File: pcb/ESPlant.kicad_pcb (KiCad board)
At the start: 2 copper layers, 43 x 23 mm, 23 parts, among them J1 Power, J2 TAG, J3 PUMP, J4 Soil Moisture, Q1 Q_NPN_BCE, Q2 Pump Driver, U1 ESP32-WROOM-32, U2 Si7021-A20, U3 LD1117S33TR_SOT223

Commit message: Increase with of pump traces to support 1A
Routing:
- net PUMP+: track 13.8 -> 14.8 mm
- net PUMP-: track 7.31 -> 8.27 mm
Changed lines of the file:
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@@
     (thickness 1.6)
     (drawings 4)
-    (tracks 157)
+    (tracks 161)
     (zones 0)
     (modules 23)
@@
   )
   (setup
-    (last_trace_width 0.25)
+    (last_trace_width 0.8)
+    (user_trace_width 0.8)
     (trace_clearance 0.2)
     (zone_clearance 0.508)
@@
     (add_net "Net-(Q1-Pad1)")
     (add_net "Net-(Q1-Pad2)")
-    (add_net "Net-(U1-Pad10)")
-    (add_net "Net-(U1-Pad13)")
-    (add_net "Net-(U1-Pad14)")
-    (add_net "Net-(U1-Pad16)")
-    (add_net "Net-(U1-Pad17)")
-    (add_net "Net-(U1-Pad18)")
-    (add_net "Net-(U1-Pad19)")
-    (add_net "Net-(U1-Pad20)")
-    (add_net "Net-(U1-Pad21)")
-    (add_net "Net-(U1-Pad22)")
-    (add_net "Net-(U1-Pad23)")
-    (add_net "Net-(U1-Pad24)")
-    (add_net "Net-(U1-Pad26)")
-    (add_net "Net-(U1-Pad27)")
-    (add_net "Net-(U1-Pad28)")
-    (add_net "Net-(U1-Pad29)")
-    (add_net "Net-(U1-Pad30)")
-    (add_net "Net-(U1-Pad31)")
-    (add_net "Net-(U1-Pad32)")
-    (add_net "Net-(U1-Pad37)")
-    (add_net "Net-(U1-Pad4)")
-    (add_net "Net-(U1-Pad5)")
-    (add_net "Net-(U2-Pad3)")
-    (add_net "Net-(U2-Pad4)")
-    (add_net "Net-(U2-Pad7)")
     (add_net PUMP+)
     (add_net PUMP-)
@@
   (segment (start 138 93.495) (end 138.75 92.745) (width 0.25) (layer F.Cu) (net 10))
   (segment (start 167.04 106.5) (end 168 106.5) (width 0.25) (layer B.Cu) (net 11))
-  (segment (start 165 104.46) (end 167.04 106.5) (width 0.25) (layer B.Cu) (net 11))
-  (segment (start 169.88 106.5) (end 171 107.62) (width 0.25) (layer B.Cu) (net 11))
-  (segment (start 168 106.5) (end 169.88 106.5) (width 0.25) (layer B.Cu) (net 11))
-  (segment (start 168.92 103) (end 168 103) (width 0.25) (layer B.Cu) (net 12))
-  (segment (start 171 105.08) (end 168.92 103) (width 0.25) (layer B.Cu) (net 12))
-  (segment (start 171 100) (end 168 103) (width 0.25) (layer B.Cu) (net 12))
-  (segment (start 167.475 98) (end 167 98) (width 0.25) (layer B.Cu) (net 12))
-  (segment (start 168 98.525) (end 167.475 98) (width 0.25) (layer B.Cu) (net 12))
-  (segment (start 168 103) (end 168 98.525) (width 0.25) (layer B.Cu) (net 12))
+  (segment (start 169.12 107.62) (end 168 106.5) (width 0.8) (layer B.Cu) (net 11))
+  (segment (start 171 107.62) (end 169.12 107.62) (width 0.8) (layer B.Cu) (net 11))
+  (segment (start 165.96 104.46) (end 168 106.5) (width 0.8) (layer B.Cu) (net 11))
+  (segment (start 165 104.46) (end 165.96 104.46) (width 0.8) (layer B.Cu) (net 11))
+  (segment (start 169.35 100) (end 168 101.35) (width 0.8) (layer B.Cu) (net 12))
+  (segment (start 168 101.35) (end 168 103) (width 0.8) (layer B.Cu) (net 12))
+  (segment (start 171 100) (end 169.35 100) (width 0.8) (layer B.Cu) (net 12))
+  (segment (start 168 102.1) (end 168 103) (width 0.25) (layer B.Cu) (net 12))
+  (segment (start 168 98.525) (end 168 102.1) (width 0.25) (layer B.Cu) (net 12))
+  (segment (start 167.475 98) (end 168 98.525) (width 0.25) (layer B.Cu) (net 12))
+  (segment (start 167 98) (end 167.475 98) (width 0.25) (layer B.Cu) (net 12))
+  (segment (start 170.08 105.08) (end 168 103) (width 0.8) (layer B.Cu) (net 12))
+  (segment (start 171 105.08) (end 170.08 105.08) (width 0.8) (layer B.Cu) (net 12))
   (via (at 159 98) (size 0.8) (drill 0.4) (layers F.Cu B.Cu) (net 13))
   (segment (start 157.875 99.125) (end 159 98) (width 0.25) (layer B.Cu) (net 13))
@@
   (segment (start 157 95.285) (end 158.715 95.285) (width 0.25) (layer F.Cu) (net 19))
   (segment (start 159 95) (end 152 95) (width 0.25) (layer B.Cu) (net 19))
+  (zone (net 1) (net_name GNDREF) (layer B.Cu) (hatch edge 0.508)
+    (connect_pads (clearance 0.508))
+    (min_thickness 0.254)
+    (fill yes (arc_segments 32) (thermal_gap 0.508) (thermal_bridge_width 0.508))
+    (polygon
+      (pts
+        (xy 177 126.5) (xy 126.5 126.5) (xy 126.5 84) (xy 177 84)
+      )
+    )
+  )
   (zone (net 1) (net_name GNDREF) (layer F.Cu) (hatch edge 0.508)
     (connect_pads (clearance 0.508))
@@
     (polygon
       (pts
-        (xy 182 126) (xy 126 126) (xy 126 79) (xy 182 79)
+        (xy 180 130.5) (xy 124.5 130.5) (xy 124.5 81) (xy 180 81)
       )
     )
-  )
-  (zone (net 1) (net_name GNDREF) (layer B.Cu) (hatch edge 0.508)
-    (connect_pads (clearance 0.508))
-    (min_thickness 0.254)
-    (fill yes (arc_segments 32) (thermal_gap 0.508) (thermal_bridge_width 0.508))
-    (polygon
-      (pts
-        (xy 184 128) (xy 124 128) (xy 124 77) (xy 184 77)
-      )
-    )

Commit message: Official revision 0.1!  Adding revision info and logo to PCB
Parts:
- added C4: 10uF, Capacitor_SMD:C_0603_1608Metric_Pad1.05x0.95mm_HandSolder, B.Cu at (169.0, 97.1)
- added G***: LOGO, Graphics:e3_6mm, B.Cu at (152.0, 100.5)
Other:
- board text added: "ESPlant - Rev 0.1 Ed Sandor 2020-03"

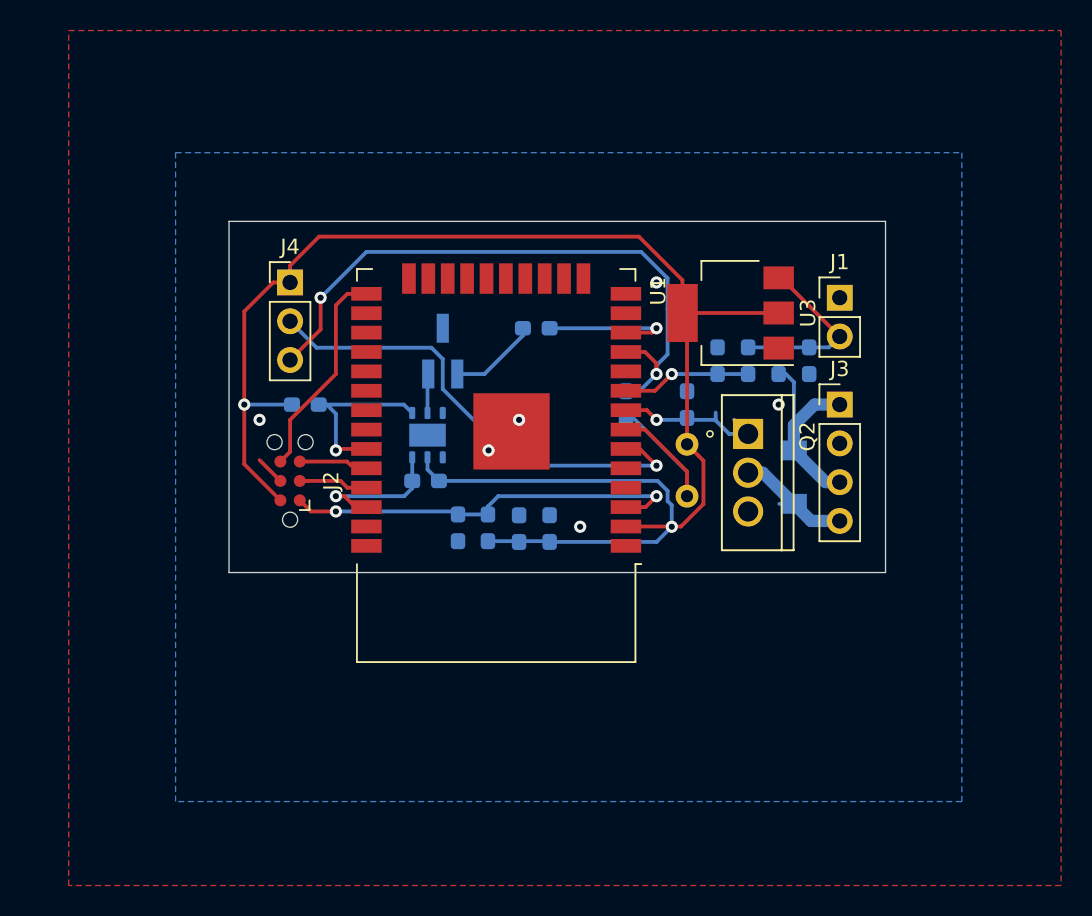
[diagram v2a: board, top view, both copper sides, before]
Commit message: PCB Revision 0.2 fixing Q1 footprint from NPN BCE to BEC to match more common parts. Minor routing revisions
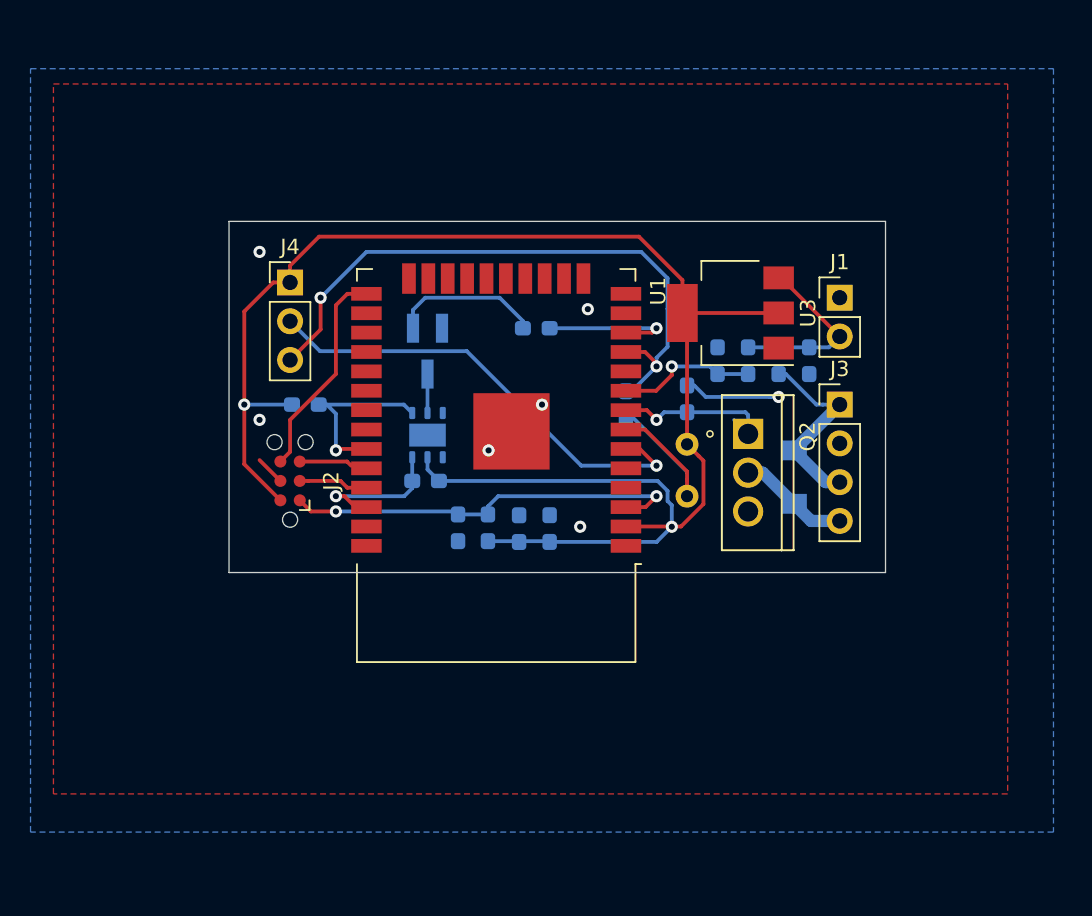
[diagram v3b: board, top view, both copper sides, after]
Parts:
- Q1: value Q_NPN_BCE -> Q_NPN_BEC
- moved Q1 1.00 mm to (144.0, 96.5), turned to 270 degrees
- moved G*** 0.50 mm to (151.5, 100.5)
- moved R5 0.38 mm to (161.0, 99.6)
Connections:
- Q1 pad 2: Net-(Q1-Pad2) -> GNDREF
- Q1 pad 3: GNDREF -> Net-(Q1-Pad3)
- U1 pad 10: (no net) -> Net-(U1-Pad10)
- U1 pad 13: (no net) -> Net-(U1-Pad13)
- U1 pad 14: (no net) -> Net-(U1-Pad14)
- U1 pad 16: (no net) -> Net-(U1-Pad16)
- U1 pad 17: (no net) -> Net-(U1-Pad17)
- U1 pad 18: (no net) -> Net-(U1-Pad18)
- U1 pad 19: (no net) -> Net-(U1-Pad19)
- U1 pad 20: (no net) -> Net-(U1-Pad20)
- U1 pad 21: (no net) -> Net-(U1-Pad21)
- U1 pad 22: (no net) -> Net-(U1-Pad22)
- U1 pad 23: (no net) -> Net-(U1-Pad23)
- U1 pad 24: (no net) -> Net-(U1-Pad24)
- U1 pad 26: (no net) -> Net-(U1-Pad26)
- U1 pad 27: (no net) -> Net-(U1-Pad27)
- U1 pad 28: (no net) -> Net-(U1-Pad28)
- U1 pad 29: (no net) -> Net-(U1-Pad29)
- U1 pad 30: (no net) -> Net-(U1-Pad30)
- U1 pad 31: (no net) -> Net-(U1-Pad31)
- U1 pad 32: (no net) -> Net-(U1-Pad32)
- U1 pad 37: (no net) -> Net-(U1-Pad37)
- U1 pad 4: (no net) -> Net-(U1-Pad4)
- U1 pad 5: (no net) -> Net-(U1-Pad5)
- U2 pad 2: Net-(Q1-Pad2) -> Net-(Q1-Pad3)
- U2 pad 3: (no net) -> Net-(U2-Pad3)
- U2 pad 4: (no net) -> Net-(U2-Pad4)
- U2 pad 7: (no net) -> Net-(U2-Pad7)
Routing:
- net GNDREF: track 2.58 -> 8.89 mm, vias 6 -> 7
- net Net-(Q1-Pad1): track 5.82 -> 9.84 mm
- net Net-(Q1-Pad2): track 2.57 -> 0.00 mm
- net Net-(Q1-Pad3): track 0.00 -> 2.55 mm
- net PUMP+: track 14.8 -> 12.9 mm
- net SOIL_ANALOG: track 31.5 -> 30.4 mm
- net PUMP-: track 8.27 -> 7.31 mm
- net SENSOR_EN: track 41.6 -> 40.8 mm
- net BATT_ANALOG: track 8.59 -> 9.34 mm
- net PUMP_EN: track 10.5 -> 11.2 mm
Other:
- board text added: "ESPlant - Rev 0.2 Ed Sandor 2020-03"
- board text removed: "ESPlant - Rev 0.1 Ed Sandor 2020-03"
